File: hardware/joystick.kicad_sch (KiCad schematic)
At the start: 0 parts

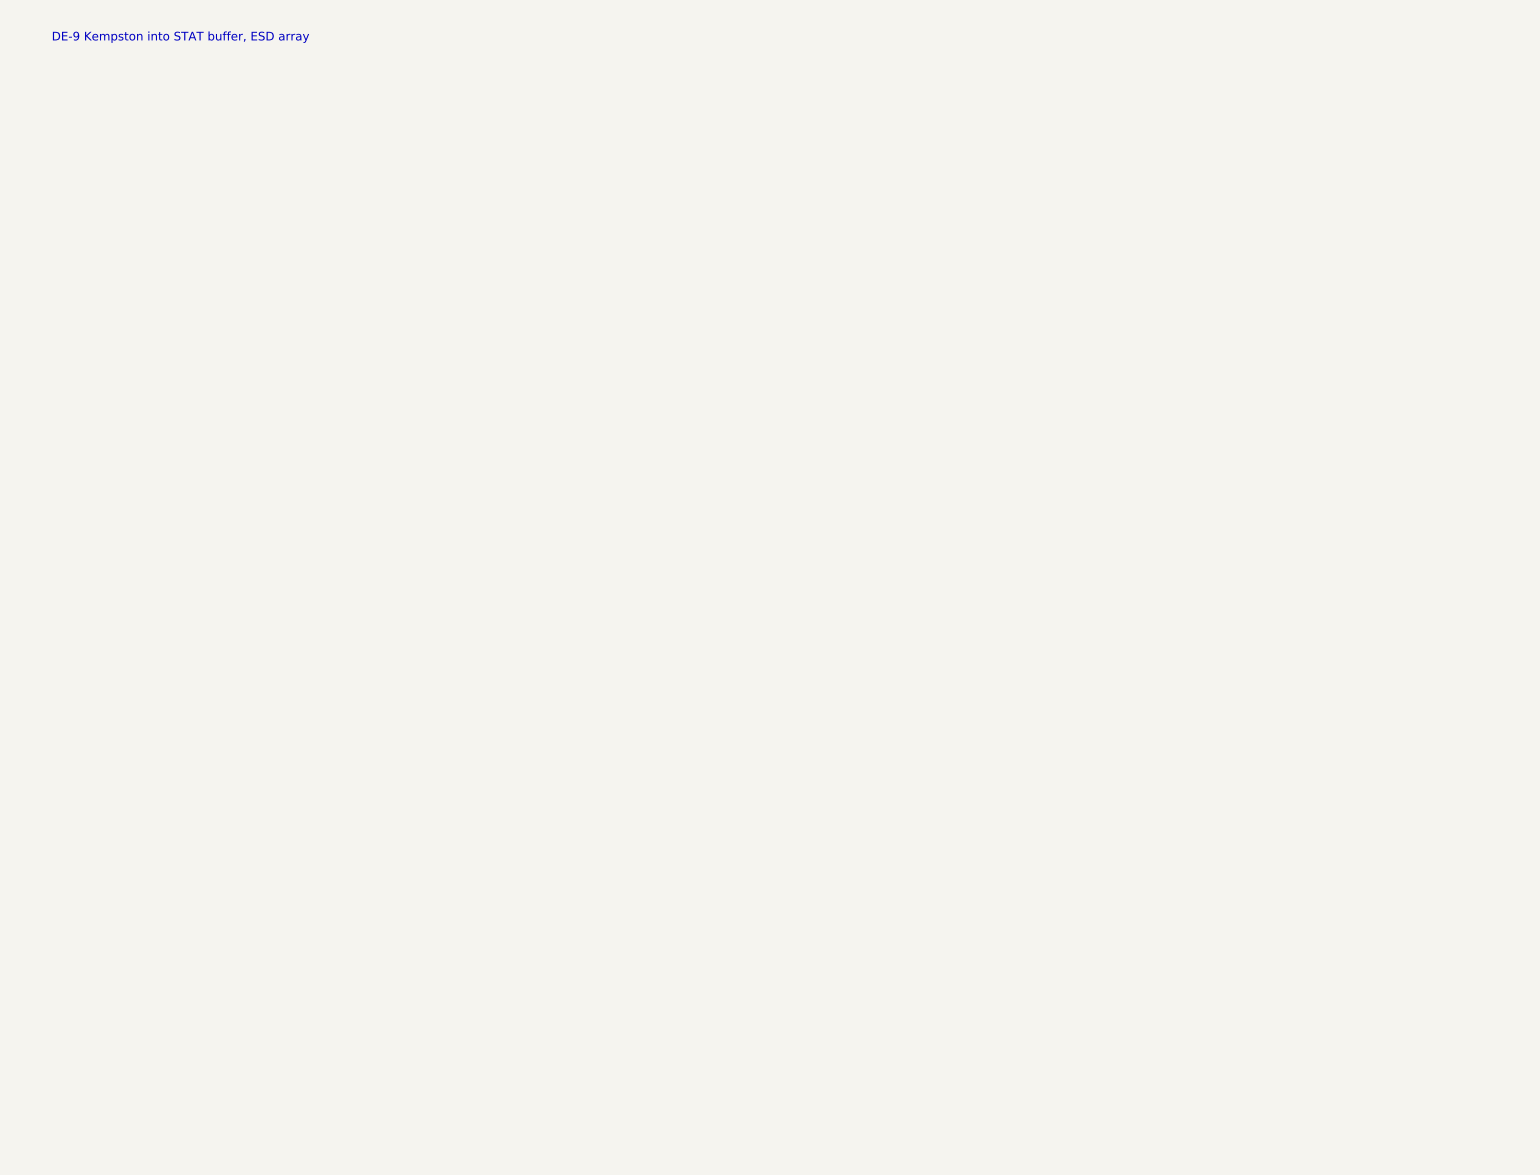
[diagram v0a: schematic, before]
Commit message: Remaining sheets: power, SD and display, WiFi, audio, joystick; ERC clean
- Power: Schottky diode-OR of edge +5V and USB VBUS (card runs from the
  2068/expansion bus, USB alone, or both), two TLV1117LV33 LDOs, bulk caps
- SD: Hirose DM3AT in SPI mode with series R, pull-ups, card detect to STAT
- OLED: 7-pin header (Waveshare 1.27in 128x96 SSD1351) on SPI1
- WiFi: ESP32-C3-WROOM-02 on UART, EN/boot from CTL, IO8 pull-up
- Audio: PWM low-pass, 2068 SOUND mix, MCP6002 buffers, 3.5 mm jack
- Joystick: DE-9 Kempston with pull-ups, series R, optional +5V jumper
- Memory sheet: activity LED on CTL bit 6
- Docs: power decision updated

Co-Authored-By: Claude Fable 5.1 <noreply@anthropic.com>
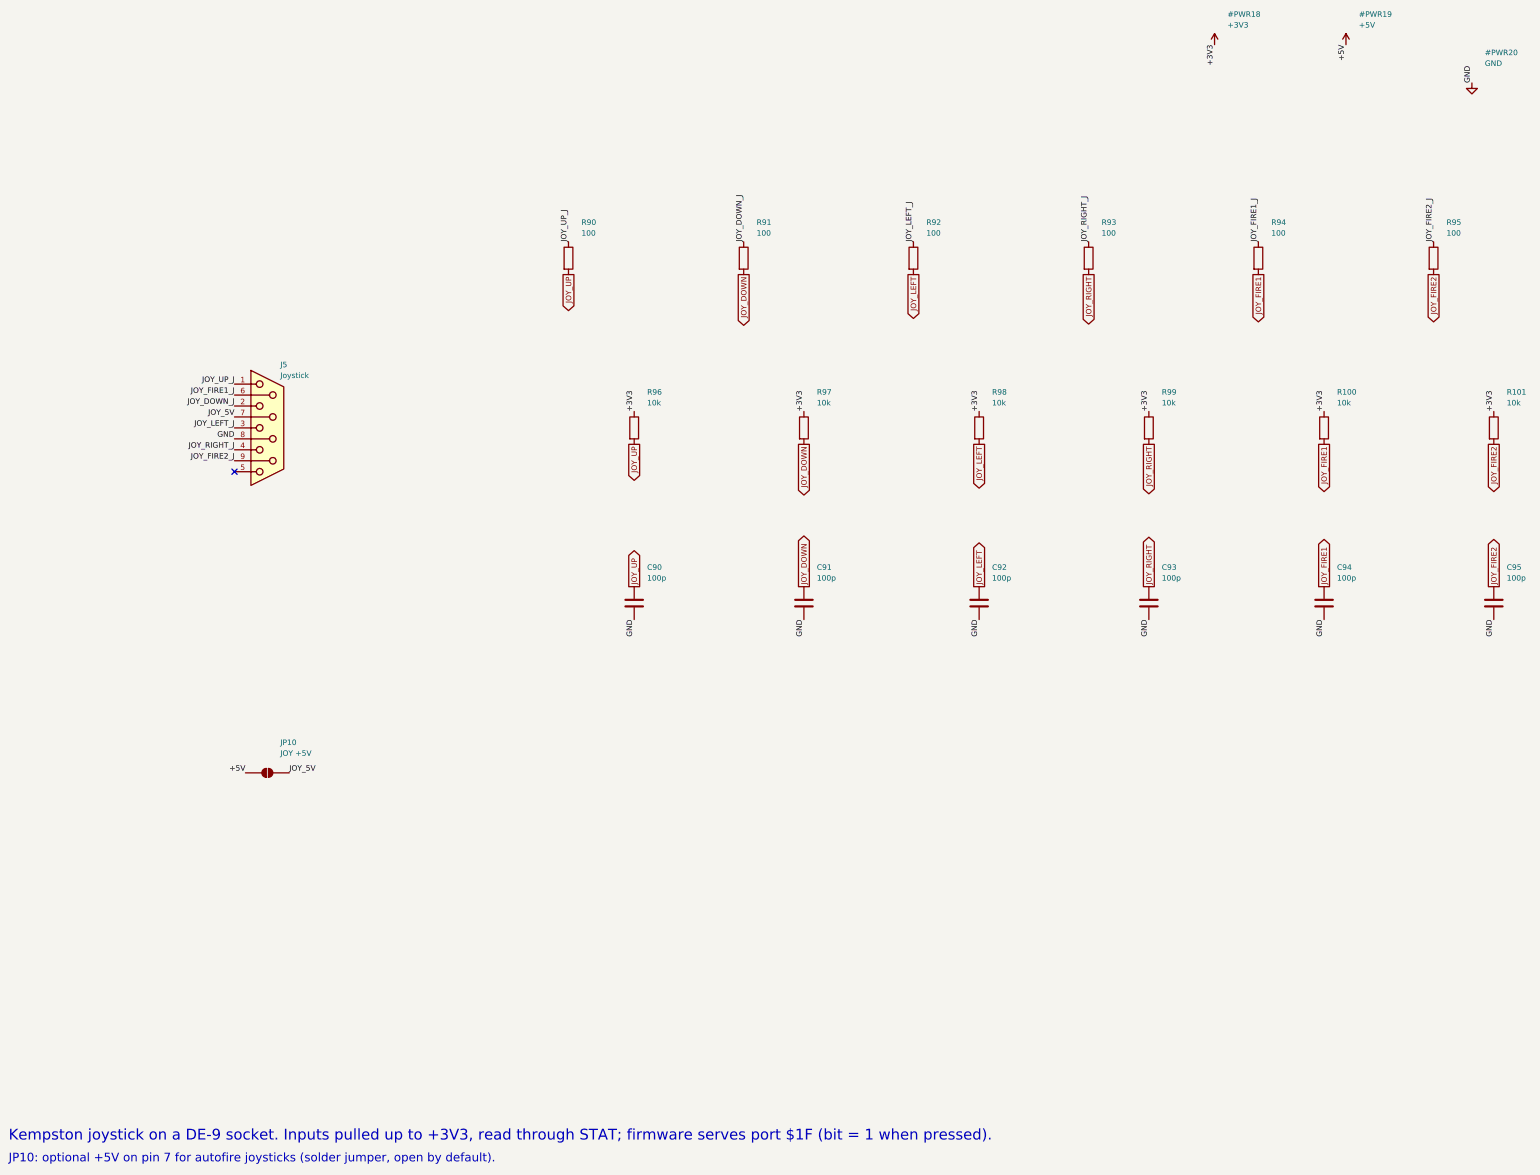
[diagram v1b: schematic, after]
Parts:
- added C90, C91, C92, C93, C94, C95: 100p, Capacitor_SMD:C_0603_1608Metric, symbol Device:C
- added J5: Joystick, Connector_Dsub:DSUB-9_Socket_Horizontal_P2.77x2.84mm_EdgePinOffset7.70mm_Housed_MountingHolesOffset9.12mm, symbol Connector:DE9_Socket
- added JP10: JOY +5V, Jumper:SolderJumper-2_P1.3mm_Open_RoundedPad1.0x1.5mm, symbol Jumper:SolderJumper_2_Open
- added R100, R101, R96, R97, R98, R99: 10k, Resistor_SMD:R_0603_1608Metric, symbol Device:R
- added R90, R91, R92, R93, R94, R95: 100, Resistor_SMD:R_0603_1608Metric, symbol Device:R
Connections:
- new net +3V3: R100.1, R101.1, R96.1, R97.1, R98.1, R99.1
- new net +5V: JP10.1 (A)
- new net GND: C90.2, C91.2, C92.2, C93.2, C94.2, C95.2, J5.8
- new net JOY_5V: J5.7, JP10.2 (B)
- new net JOY_DOWN: C91.1, R91.2, R97.2
- new net JOY_DOWN_J: J5.2, R91.1
- new net JOY_FIRE1: C94.1, R100.2, R94.2
- new net JOY_FIRE1_J: J5.6, R94.1
- new net JOY_FIRE2: C95.1, R101.2, R95.2
- new net JOY_FIRE2_J: J5.9, R95.1
- new net JOY_LEFT: C92.1, R92.2, R98.2
- new net JOY_LEFT_J: J5.3, R92.1
- new net JOY_RIGHT: C93.1, R93.2, R99.2
- new net JOY_RIGHT_J: J5.4, R93.1
- new net JOY_UP: C90.1, R90.2, R96.2
- new net JOY_UP_J: J5.1, R90.1
- no-connect marks 0 -> 1
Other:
- note added: "JP10: optional +5V on pin 7 for autofire joysticks (solder jumper, open by default)."
- note added: "Kempston joystick on a DE-9 socket. Inputs pulled up to +3V3, read through STAT; firmware serves port $1F (bit = 1 when pressed)."
- note removed: "DE-9 Kempston into STAT buffer, ESD array"

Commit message: BOM pass: LCSC and MPN fields on every part, JLCPCB BOM export
- scripts/parts.py: part table looked up 2026-09-16; schlib stamps fields
- substitutions for stock: 74HC273PW, 74LVC139PW, TI LVC04/08/126/574/1G86,
  33R USB series, XKB TS-1187A switches, Panasonic polymer 220uF, B5819W
- bom/: JLCPCB-format and full BOM CSVs

Co-Authored-By: Claude Fable 5.1 <noreply@anthropic.com>
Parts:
- C90, C91, C92, C93, C94, C95: LCSC (none) -> C14858; MPN (none) -> CL10C101JB8NNNC
- J5: LCSC (none) -> C75749; MPN (none) -> DS1037-09FNAKT74-0CC
- R100, R101, R96, R97, R98, R99: LCSC (none) -> C25804; MPN (none) -> 0603WAF1002T5E
- R90, R91, R92, R93, R94, R95: LCSC (none) -> C22775; MPN (none) -> 0603WAF1000T5E
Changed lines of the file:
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@@
     (property "Datasheet" "" (at 80.01 119.38 0) (effects (font (size 1.27 1.27)) (justify left) (hide yes)))
     (property "Description" "" (at 80.01 119.38 0) (effects (font (size 1.27 1.27)) (justify left) (hide yes)))
+    (property "MPN" "DS1037-09FNAKT74-0CC" (at 80.01 119.38 0) (effects (font (size 1.27 1.27)) (justify left) (hide yes)))
+    (property "LCSC" "C75749" (at 80.01 119.38 0) (effects (font (size 1.27 1.27)) (justify left) (hide yes)))
     (pin "1")
     (pin "2")
@@
     (property "Datasheet" "" (at 149.86 80.01 0) (effects (font (size 1.27 1.27)) (justify left) (hide yes)))
     (property "Description" "" (at 149.86 80.01 0) (effects (font (size 1.27 1.27)) (justify left) (hide yes)))
+    (property "MPN" "0603WAF1000T5E" (at 149.86 80.01 0) (effects (font (size 1.27 1.27)) (justify left) (hide yes)))
+    (property "LCSC" "C22775" (at 149.86 80.01 0) (effects (font (size 1.27 1.27)) (justify left) (hide yes)))
     (pin "1")
     (pin "2")
@@
     (property "Datasheet" "" (at 165.1 119.38 0) (effects (font (size 1.27 1.27)) (justify left) (hide yes)))
     (property "Description" "" (at 165.1 119.38 0) (effects (font (size 1.27 1.27)) (justify left) (hide yes)))
+    (property "MPN" "0603WAF1002T5E" (at 165.1 119.38 0) (effects (font (size 1.27 1.27)) (justify left) (hide yes)))
+    (property "LCSC" "C25804" (at 165.1 119.38 0) (effects (font (size 1.27 1.27)) (justify left) (hide yes)))
     (pin "1")
     (pin "2")
@@
     (property "Datasheet" "" (at 165.1 160.02 0) (effects (font (size 1.27 1.27)) (justify left) (hide yes)))
     (property "Description" "" (at 165.1 160.02 0) (effects (font (size 1.27 1.27)) (justify left) (hide yes)))
+    (property "MPN" "CL10C101JB8NNNC" (at 165.1 160.02 0) (effects (font (size 1.27 1.27)) (justify left) (hide yes)))
+    (property "LCSC" "C14858" (at 165.1 160.02 0) (effects (font (size 1.27 1.27)) (justify left) (hide yes)))
     (pin "1")
     (pin "2")
@@
     (property "Datasheet" "" (at 190.5 80.01 0) (effects (font (size 1.27 1.27)) (justify left) (hide yes)))
     (property "Description" "" (at 190.5 80.01 0) (effects (font (size 1.27 1.27)) (justify left) (hide yes)))
+    (property "MPN" "0603WAF1000T5E" (at 190.5 80.01 0) (effects (font (size 1.27 1.27)) (justify left) (hide yes)))
+    (property "LCSC" "C22775" (at 190.5 80.01 0) (effects (font (size 1.27 1.27)) (justify left) (hide yes)))
     (pin "1")
     (pin "2")
@@
     (property "Datasheet" "" (at 204.47 119.38 0) (effects (font (size 1.27 1.27)) (justify left) (hide yes)))
     (property "Description" "" (at 204.47 119.38 0) (effects (font (size 1.27 1.27)) (justify left) (hide yes)))
+    (property "MPN" "0603WAF1002T5E" (at 204.47 119.38 0) (effects (font (size 1.27 1.27)) (justify left) (hide yes)))
+    (property "LCSC" "C25804" (at 204.47 119.38 0) (effects (font (size 1.27 1.27)) (justify left) (hide yes)))
     (pin "1")
     (pin "2")
@@
     (property "Datasheet" "" (at 204.47 160.02 0) (effects (font (size 1.27 1.27)) (justify left) (hide yes)))
     (property "Description" "" (at 204.47 160.02 0) (effects (font (size 1.27 1.27)) (justify left) (hide yes)))
+    (property "MPN" "CL10C101JB8NNNC" (at 204.47 160.02 0) (effects (font (size 1.27 1.27)) (justify left) (hide yes)))
+    (property "LCSC" "C14858" (at 204.47 160.02 0) (effects (font (size 1.27 1.27)) (justify left) (hide yes)))
     (pin "1")
     (pin "2")
@@
     (property "Datasheet" "" (at 229.87 80.01 0) (effects (font (size 1.27 1.27)) (justify left) (hide yes)))
     (property "Description" "" (at 229.87 80.01 0) (effects (font (size 1.27 1.27)) (justify left) (hide yes)))
+    (property "MPN" "0603WAF1000T5E" (at 229.87 80.01 0) (effects (font (size 1.27 1.27)) (justify left) (hide yes)))
+    (property "LCSC" "C22775" (at 229.87 80.01 0) (effects (font (size 1.27 1.27)) (justify left) (hide yes)))
     (pin "1")
     (pin "2")
@@
     (property "Datasheet" "" (at 245.11 119.38 0) (effects (font (size 1.27 1.27)) (justify left) (hide yes)))
     (property "Description" "" (at 245.11 119.38 0) (effects (font (size 1.27 1.27)) (justify left) (hide yes)))
+    (property "MPN" "0603WAF1002T5E" (at 245.11 119.38 0) (effects (font (size 1.27 1.27)) (justify left) (hide yes)))
+    (property "LCSC" "C25804" (at 245.11 119.38 0) (effects (font (size 1.27 1.27)) (justify left) (hide yes)))
     (pin "1")
     (pin "2")
@@
     (property "Datasheet" "" (at 245.11 160.02 0) (effects (font (size 1.27 1.27)) (justify left) (hide yes)))
     (property "Description" "" (at 245.11 160.02 0) (effects (font (size 1.27 1.27)) (justify left) (hide yes)))
+    (property "MPN" "CL10C101JB8NNNC" (at 245.11 160.02 0) (effects (font (size 1.27 1.27)) (justify left) (hide yes)))
+    (property "LCSC" "C14858" (at 245.11 160.02 0) (effects (font (size 1.27 1.27)) (justify left) (hide yes)))
     (pin "1")
     (pin "2")
@@
     (property "Datasheet" "" (at 270.51 80.01 0) (effects (font (size 1.27 1.27)) (justify left) (hide yes)))
     (property "Description" "" (at 270.51 80.01 0) (effects (font (size 1.27 1.27)) (justify left) (hide yes)))
+    (property "MPN" "0603WAF1000T5E" (at 270.51 80.01 0) (effects (font (size 1.27 1.27)) (justify left) (hide yes)))
+    (property "LCSC" "C22775" (at 270.51 80.01 0) (effects (font (size 1.27 1.27)) (justify left) (hide yes)))
     (pin "1")
     (pin "2")
@@
     (property "Datasheet" "" (at 284.48 119.38 0) (effects (font (size 1.27 1.27)) (justify left) (hide yes)))
     (property "Description" "" (at 284.48 119.38 0) (effects (font (size 1.27 1.27)) (justify left) (hide yes)))
+    (property "MPN" "0603WAF1002T5E" (at 284.48 119.38 0) (effects (font (size 1.27 1.27)) (justify left) (hide yes)))
+    (property "LCSC" "C25804" (at 284.48 119.38 0) (effects (font (size 1.27 1.27)) (justify left) (hide yes)))
     (pin "1")
     (pin "2")
@@
     (property "Datasheet" "" (at 284.48 160.02 0) (effects (font (size 1.27 1.27)) (justify left) (hide yes)))
     (property "Description" "" (at 284.48 160.02 0) (effects (font (size 1.27 1.27)) (justify left) (hide yes)))
+    (property "MPN" "CL10C101JB8NNNC" (at 284.48 160.02 0) (effects (font (size 1.27 1.27)) (justify left) (hide yes)))
+    (property "LCSC" "C14858" (at 284.48 160.02 0) (effects (font (size 1.27 1.27)) (justify left) (hide yes)))
     (pin "1")
     (pin "2")
@@
     (property "Datasheet" "" (at 309.88 80.01 0) (effects (font (size 1.27 1.27)) (justify left) (hide yes)))
     (property "Description" "" (at 309.88 80.01 0) (effects (font (size 1.27 1.27)) (justify left) (hide yes)))
+    (property "MPN" "0603WAF1000T5E" (at 309.88 80.01 0) (effects (font (size 1.27 1.27)) (justify left) (hide yes)))
+    (property "LCSC" "C22775" (at 309.88 80.01 0) (effects (font (size 1.27 1.27)) (justify left) (hide yes)))
     (pin "1")
     (pin "2")
@@
     (property "Datasheet" "" (at 325.12 119.38 0) (effects (font (size 1.27 1.27)) (justify left) (hide yes)))
     (property "Description" "" (at 325.12 119.38 0) (effects (font (size 1.27 1.27)) (justify left) (hide yes)))
+    (property "MPN" "0603WAF1002T5E" (at 325.12 119.38 0) (effects (font (size 1.27 1.27)) (justify left) (hide yes)))
+    (property "LCSC" "C25804" (at 325.12 119.38 0) (effects (font (size 1.27 1.27)) (justify left) (hide yes)))
     (pin "1")
     (pin "2")
@@
     (property "Datasheet" "" (at 325.12 160.02 0) (effects (font (size 1.27 1.27)) (justify left) (hide yes)))
     (property "Description" "" (at 325.12 160.02 0) (effects (font (size 1.27 1.27)) (justify left) (hide yes)))
+    (property "MPN" "CL10C101JB8NNNC" (at 325.12 160.02 0) (effects (font (size 1.27 1.27)) (justify left) (hide yes)))
+    (property "LCSC" "C14858" (at 325.12 160.02 0) (effects (font (size 1.27 1.27)) (justify left) (hide yes)))
     (pin "1")
     (pin "2")
@@
     (property "Datasheet" "" (at 350.52 80.01 0) (effects (font (size 1.27 1.27)) (justify left) (hide yes)))
     (property "Description" "" (at 350.52 80.01 0) (effects (font (size 1.27 1.27)) (justify left) (hide yes)))
+    (property "MPN" "0603WAF1000T5E" (at 350.52 80.01 0) (effects (font (size 1.27 1.27)) (justify left) (hide yes)))
+    (property "LCSC" "C22775" (at 350.52 80.01 0) (effects (font (size 1.27 1.27)) (justify left) (hide yes)))
     (pin "1")
     (pin "2")
@@
     (property "Datasheet" "" (at 364.49 119.38 0) (effects (font (size 1.27 1.27)) (justify left) (hide yes)))
     (property "Description" "" (at 364.49 119.38 0) (effects (font (size 1.27 1.27)) (justify left) (hide yes)))
+    (property "MPN" "0603WAF1002T5E" (at 364.49 119.38 0) (effects (font (size 1.27 1.27)) (justify left) (hide yes)))
+    (property "LCSC" "C25804" (at 364.49 119.38 0) (effects (font (size 1.27 1.27)) (justify left) (hide yes)))
     (pin "1")
     (pin "2")
@@
     (property "Datasheet" "" (at 364.49 160.02 0) (effects (font (size 1.27 1.27)) (justify left) (hide yes)))
     (property "Description" "" (at 364.49 160.02 0) (effects (font (size 1.27 1.27)) (justify left) (hide yes)))
-    (pin "1")
-    (pin "2")
+    (property "MPN" "CL10C101JB8NNNC" (at 364.49 160.02 0) (effects (font (size 1.27 1.27)) (justify left) (hide yes)))
+    (property "LCSC" "C14858" (at 364.49 160.02 0) (effects (font (size 1.27 1.27)) (justify left) (hide yes)))
+    (pin "1")
+    (pin "2")
